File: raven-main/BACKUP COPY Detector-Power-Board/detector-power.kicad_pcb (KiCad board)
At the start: 2 copper layers, 37 x 52.5 mm, 43 parts, among them J1 DeployLipo, J2 Conn_01x06, J9 UCLipo, Q1 CSD18543Q3A, Q2 CSD18543Q3A, U2 TPS43060RTE, U7 TPS7A4701xRGW, U8 TPS7A4701xRGW

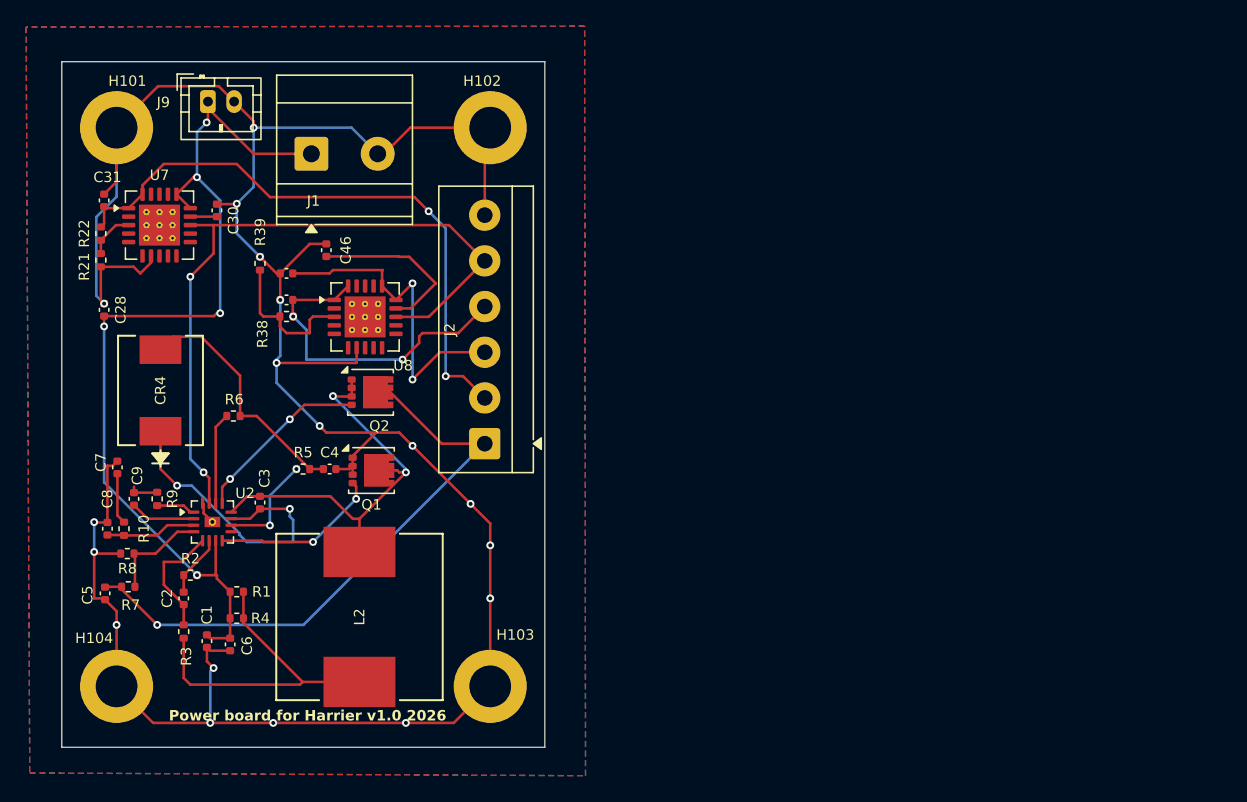
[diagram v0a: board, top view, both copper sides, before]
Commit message: Replaced buck boost
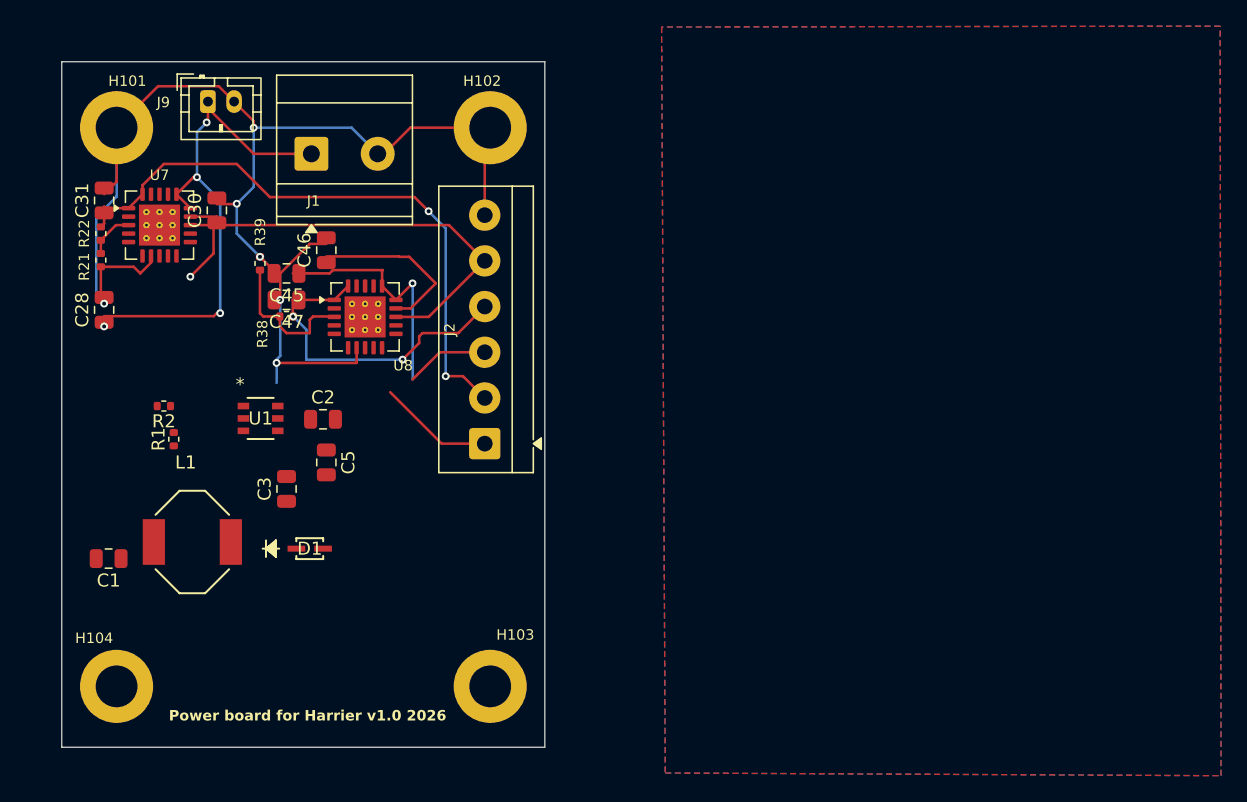
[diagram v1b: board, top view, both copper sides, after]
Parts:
- removed C4: 10u, Capacitor_SMD:C_0402_1005Metric
- removed C6: 22u, Capacitor_SMD:C_0402_1005Metric
- removed C7: 8.2n, Capacitor_SMD:C_0402_1005Metric
- removed C8: 470pF, Capacitor_SMD:C_0402_1005Metric
- removed C9: 4.7n, Capacitor_SMD:C_0402_1005Metric
- removed CR4: SL43-E3/57T, SL43-E3-57T:DIODE_DO214AB
- removed L2: DR127-3R3-R, DR127-3R3-R:DR127
- removed Q1, Q2: CSD18543Q3A, Package_SON:VSON-8_3.3x3.3mm_P0.65mm_NexFET
- removed R10: 6.34k, Resistor_SMD:R_0402_1005Metric
- removed R3: 10, Resistor_SMD:R_0402_1005Metric
- removed R4: 7m, Resistor_SMD:R_0402_1005Metric
- removed R5: 2, Resistor_SMD:R_0402_1005Metric
- removed R6: 100k, Resistor_SMD:R_0402_1005Metric
- removed R7: 191k, Resistor_SMD:R_0402_1005Metric
- removed R8: 11k, Resistor_SMD:R_0402_1005Metric
- removed R9: 105k, Resistor_SMD:R_0402_1005Metric
- removed U2: TPS43060RTE, Package_DFN_QFN:Texas_RTE_WQFN-16-1EP_3x3mm_P0.5mm_EP1.2x0.8mm_ThermalVias
- added D1: D_Schottky, PMEG4010BEA:SOD323F_NEX, F.Cu at (129.8, 94.7)
- added L1: 8.2u, CDR7D28MNNP-8R0NC:IND_8R0NC_SUM, F.Cu at (120.8, 94.2)
- added U1: LT8330IS6-TRMPBF, LT8330IS6:IC6_LT8330IS6-TRMPBF_ADI, F.Cu at (126.0, 84.8)
- C1: value 100n -> 4.7u; footprint Capacitor_SMD:C_0402_1005Metric -> Capacitor_SMD:C_0805_2012Metric
- C2: value 100p -> 1u; footprint Capacitor_SMD:C_0402_1005Metric -> Capacitor_SMD:C_0805_2012Metric
- C28, C30, C31, C45, C46, C47: footprint Capacitor_SMD:C_0402_1005Metric -> Capacitor_SMD:C_0805_2012Metric
- C3: value 100n -> 4.7p; footprint Capacitor_SMD:C_0402_1005Metric -> Capacitor_SMD:C_0805_2012Metric
- C5: value 10u -> 4.7u; footprint Capacitor_SMD:C_0402_1005Metric -> Capacitor_SMD:C_0805_2012Metric
- R1: value 7m -> 147k
- R2: value 10 -> 10k
- moved C5 19.7 mm to (131.1, 88.1)
- moved C2 17.4 mm to (130.8, 84.8), turned to 0 degrees
- moved R2 13.1 mm to (118.6, 83.8), turned to 180 degrees
- moved R1 12.6 mm to (119.4, 86.4), turned to 90 degrees
- moved C1 9.83 mm to (114.4, 95.5), turned to 180 degrees
- moved C3 2.29 mm to (128.0, 90.2), turned to 90 degrees
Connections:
- C2 pad 1: Net-(U2-ISNS+) -> Net-(U1-INTVCC)
- C2 pad 2: Net-(U2-ISNS–) -> GND
- C3 pad 1: Net-(Q1-D) -> /Power_Out_25V
- C3 pad 2: Net-(U2-BOOT) -> Net-(U1-FBX)
- R1 pad 1: /BBIN -> /Power_Out_25V
- R1 pad 2: Net-(L2-Pad1) -> Net-(U1-FBX)
- R2 pad 1: Net-(U2-ISNS+) -> Net-(U1-FBX)
- R2 pad 2: /BBIN -> GND
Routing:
- net GND: track 206.3 -> 103.3 mm, vias 18 -> 6
- net /Power_Out_25V: track 46.2 -> 8.87 mm, vias 1 -> 0
- net /BBIN: track 73.9 -> 40.6 mm, vias 5 -> 4
- net Net-(Q1-D): track 31.8 -> 0.00 mm, vias 2 -> 0
- net Net-(L2-Pad1): track 25.6 -> 0.00 mm
- net Net-(U2-BOOT): track 22.9 -> 0.00 mm, vias 2 -> 0
- net Net-(C4-Pad1): track 18.9 -> 0.00 mm
- net /ON-OFF: track 54.9 -> 37.0 mm, vias 2 -> 1
- net Net-(Q2-G): track 13.8 -> 0.00 mm, vias 2 -> 0
- net Net-(Q1-G): track 13.0 -> 0.00 mm, vias 2 -> 0
- net Net-(U2-ISNS–): track 9.10 -> 0.00 mm
- net Net-(U2-VCC): track 8.13 -> 0.00 mm, vias 2 -> 0
- net Net-(U2-FB): track 7.83 -> 0.00 mm
- net Net-(U2-PGOOD): track 7.03 -> 0.00 mm
- net Net-(U2-COMP): track 6.94 -> 0.00 mm
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
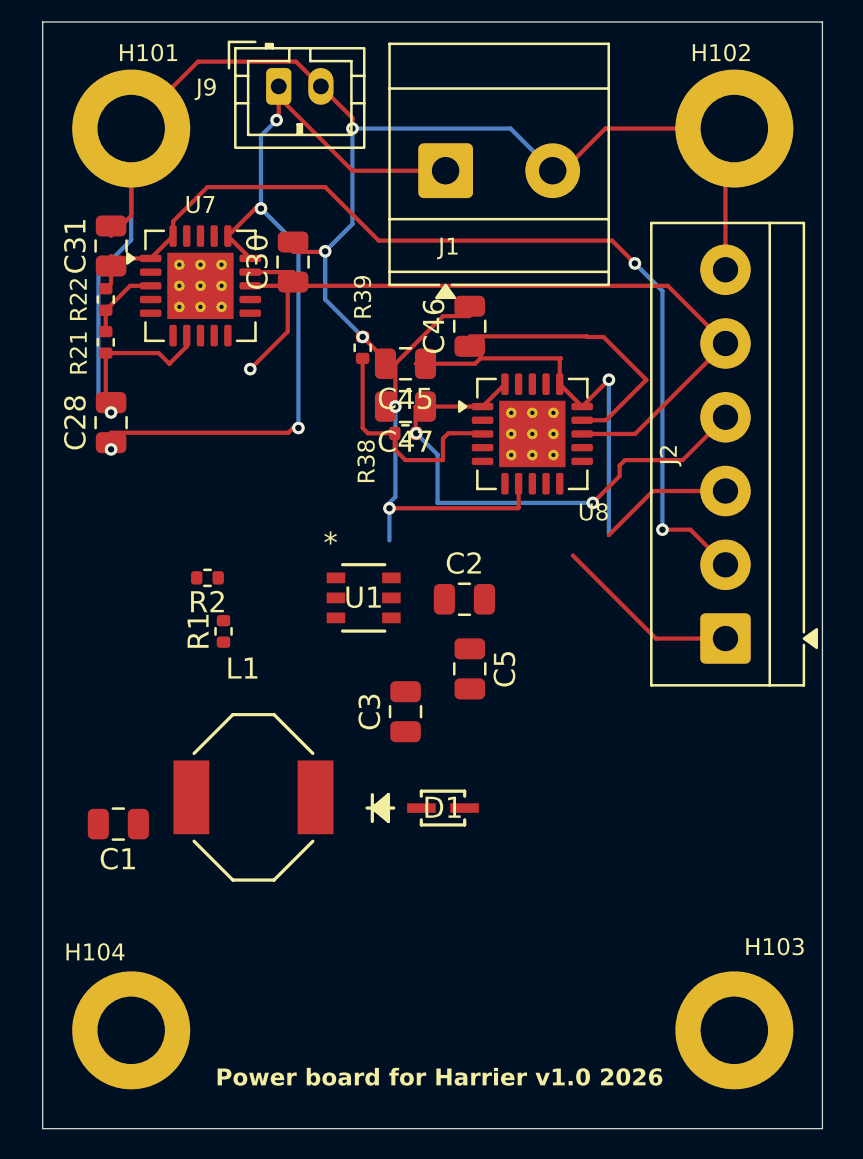
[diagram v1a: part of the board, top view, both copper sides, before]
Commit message: Completed traces for the new buckboost
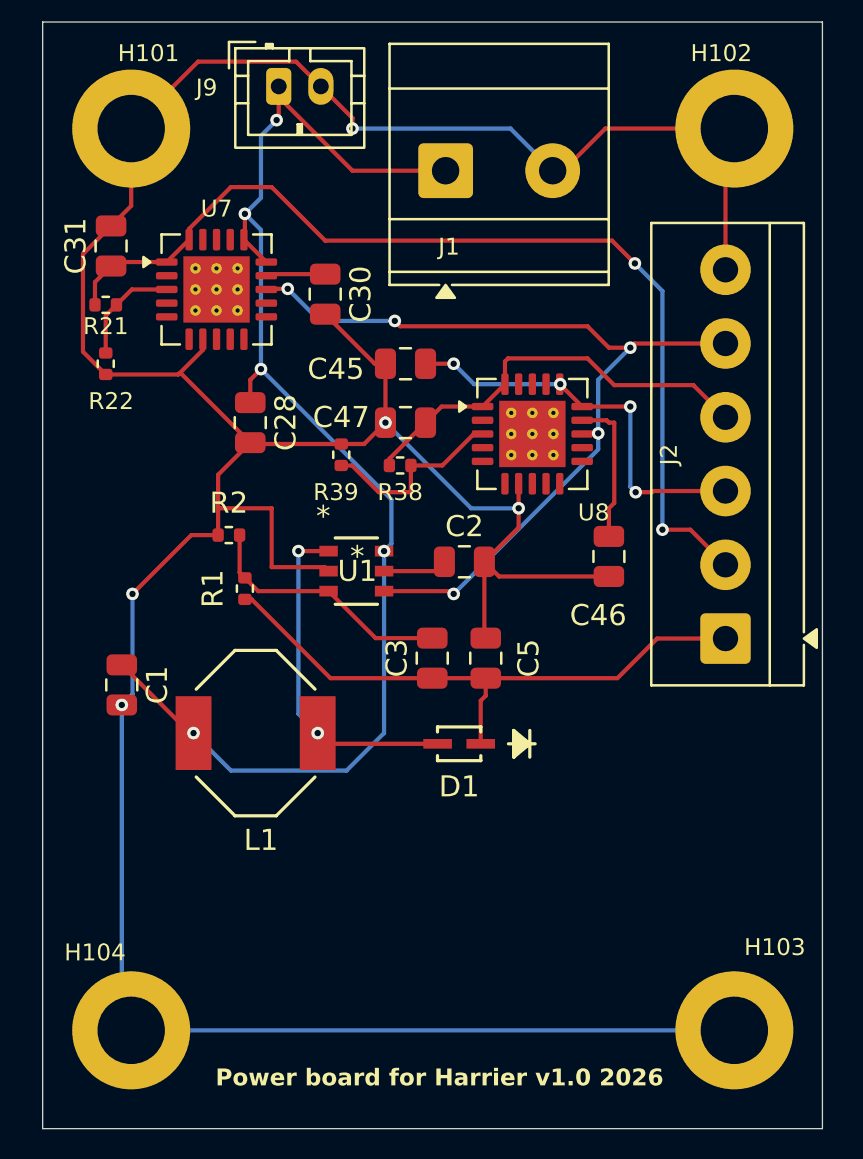
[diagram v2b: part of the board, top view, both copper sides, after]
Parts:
- moved C46 12.8 mm to (137.7, 82.8), turned to -90 degrees
- moved C1 6.61 mm to (114.6, 88.9), turned to -90 degrees
- moved C28 6.60 mm to (120.7, 76.5), turned to -90 degrees
- moved R39 5.18 mm to (125.0, 78.0)
- moved D1 3.14 mm to (130.6, 91.7), turned to 180 degrees
- moved L1 3.05 mm to (120.9, 91.2)
- moved C3 2.84 mm to (129.3, 87.6)
- moved R1 2.27 mm to (120.4, 84.3)
- moved R2 2.27 mm to (119.6, 81.8)
- moved C30 2.16 mm to (124.2, 70.4), turned to -90 degrees
- moved C2 1.78 mm to (130.8, 83.1)
- moved R38 1.55 mm to (127.8, 78.5), turned to 0 degrees
- moved U1 1.32 mm to (125.7, 83.5)
- moved R22 1.02 mm to (113.8, 73.7)
- moved C5 0.91 mm to (131.8, 87.6), turned to 90 degrees
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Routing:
- net GND: track 103.3 -> 167.8 mm, vias 6 -> 5
- net /BBIN: track 40.6 -> 64.1 mm, vias 4 -> 5
- net /Power_Out_25V: track 8.87 -> 28.3 mm
- net Net-(D1-A): track 0.00 -> 16.3 mm, vias 0 -> 2
- net Net-(U1-FBX): track 0.00 -> 12.2 mm
- net /Data_In_5V: track 25.3 -> 19.0 mm, vias 1 -> 4
- net Net-(U8-NR): track 13.1 -> 7.08 mm
- net /ON-OFF: track 37.0 -> 42.3 mm, vias 1 -> 5
- net /Data_Out_3V3: track 25.3 -> 20.0 mm, vias 2 -> 0
- net Net-(U1-INTVCC): track 0.00 -> 3.04 mm
- net Net-(U8-SENSE/FB): track 11.2 -> 9.12 mm
- net Net-(U7-SENSE/FB): track 3.63 -> 5.18 mm
- net Net-(U7-NR): track 2.07 -> 2.83 mm
- net /Power_Out_5V: track 46.7 -> 47.2 mm
